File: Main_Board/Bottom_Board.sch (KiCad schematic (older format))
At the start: 18 parts, among them P1 CONN_01X08, P2 CONN_01X08, U2 DYS_mini_ESC, U3 DYS_mini_ESC, U4 DYS_mini_ESC, U5 DYS_mini_ESC, U7 AL8805W5

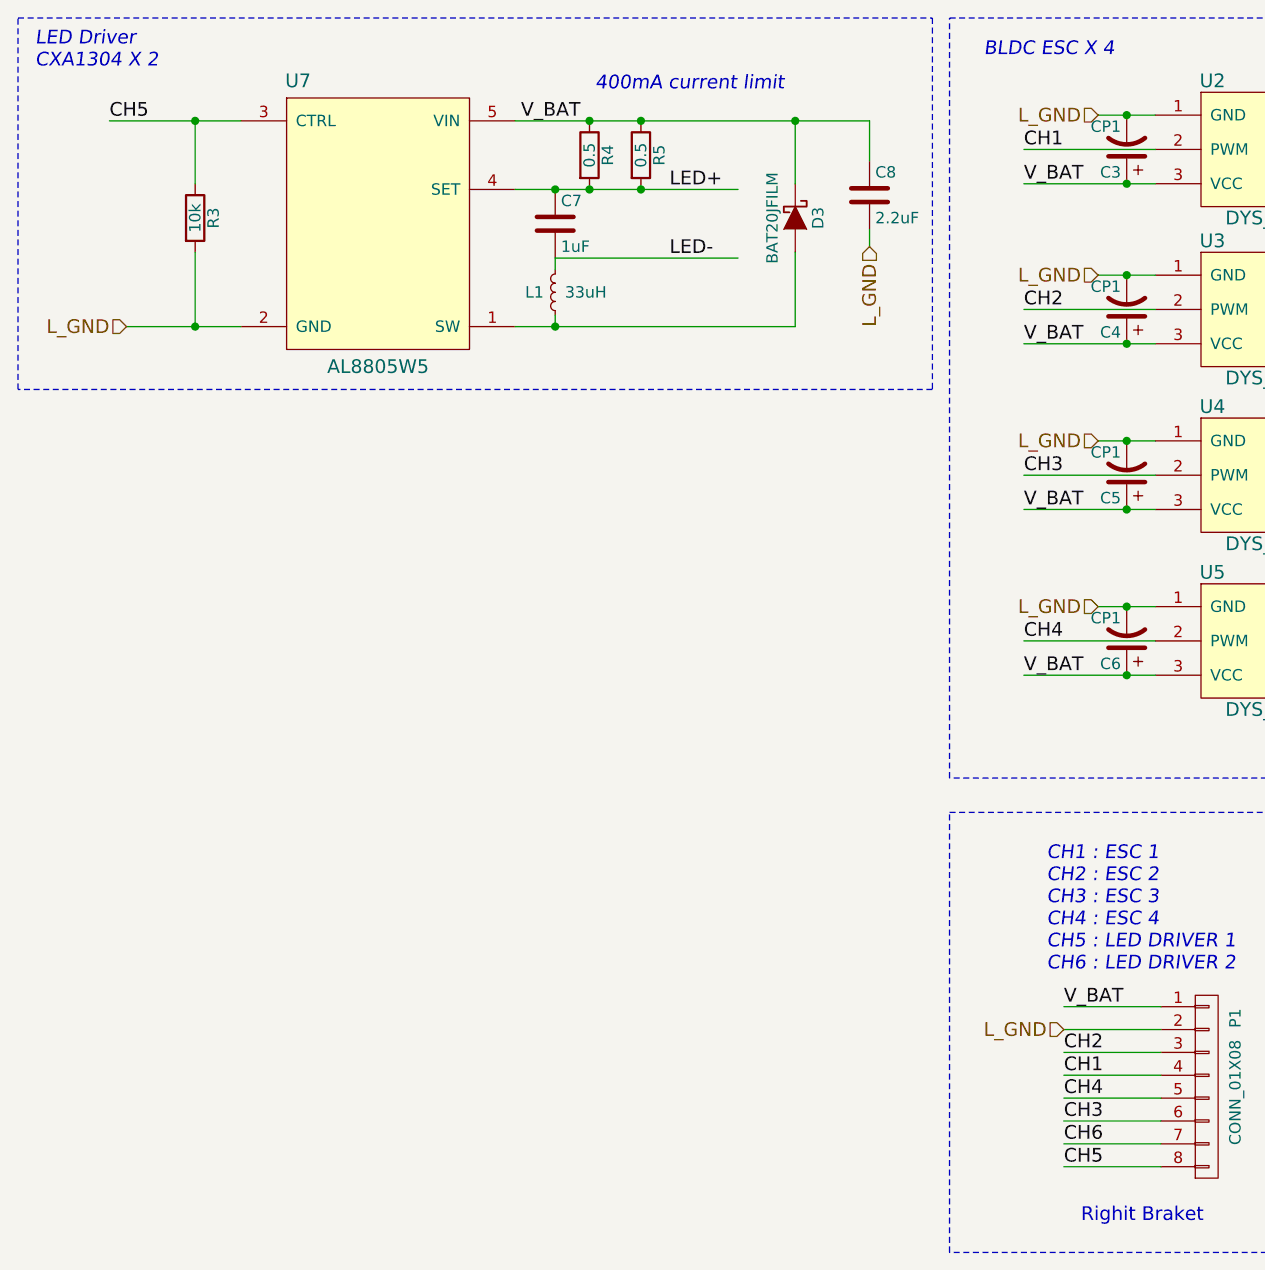
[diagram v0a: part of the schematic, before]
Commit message: Main Board : Recover LED driver USB Dist Board : Delete ADC voltage divider
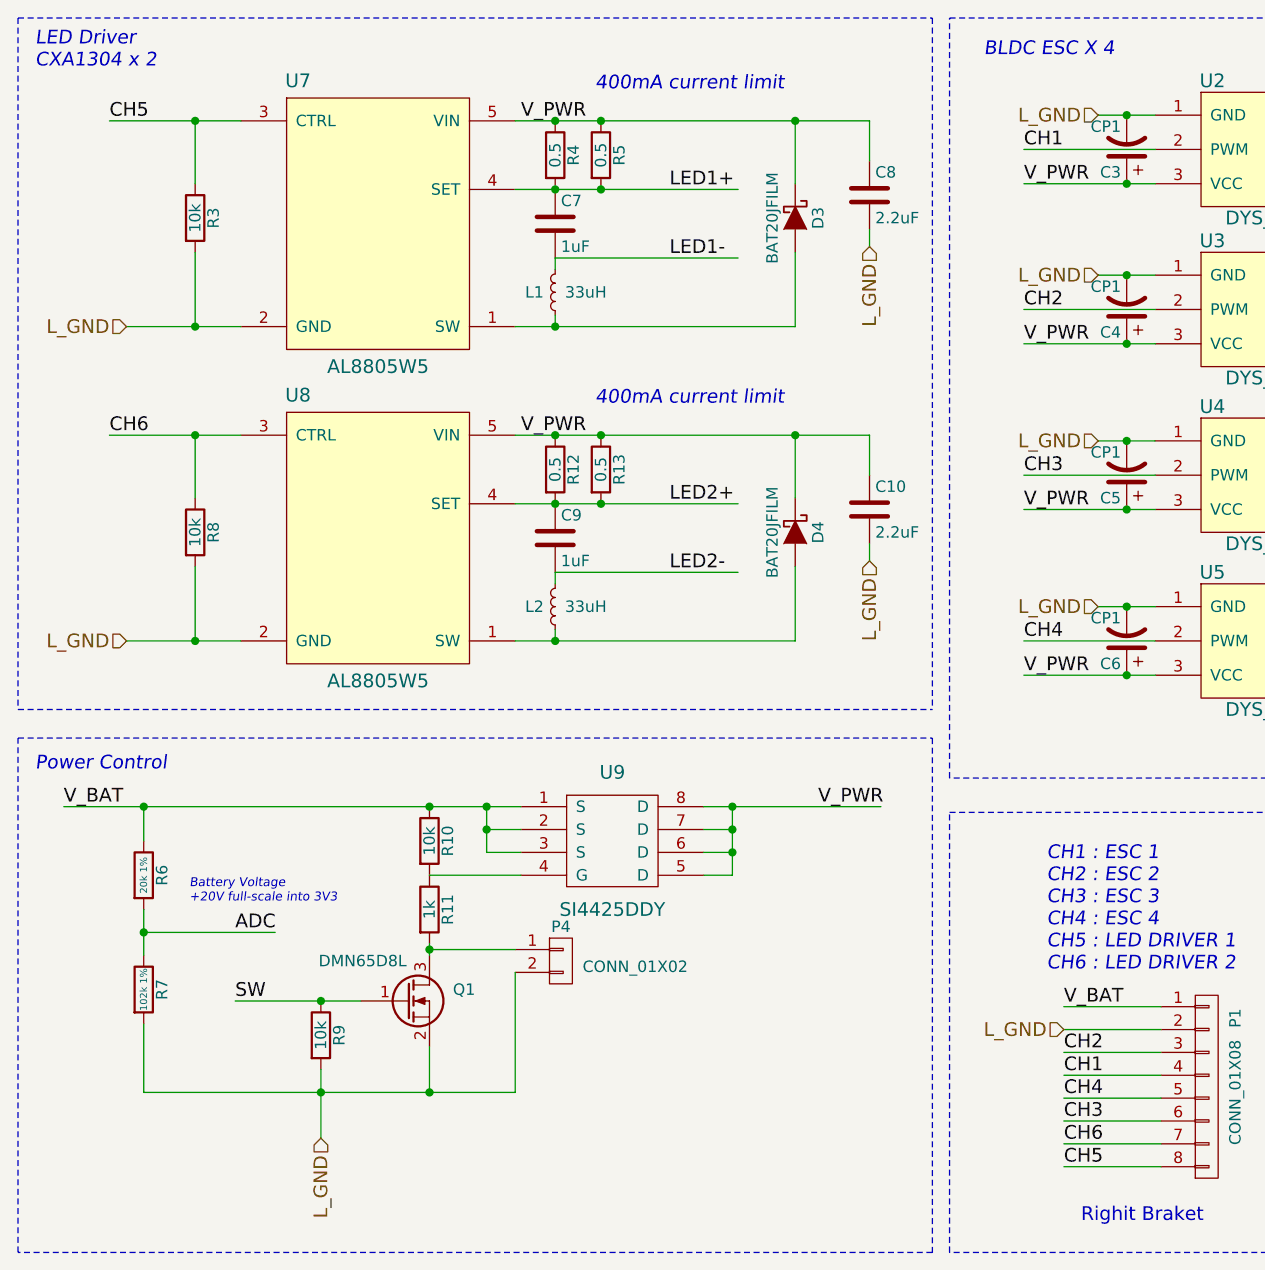
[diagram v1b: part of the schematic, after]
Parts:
- added C10: 2.2uF, Capacitors_SMD:C_0805, symbol C
- added C9: 1uF, Capacitors_SMD:C_0805, symbol C
- added D4: BAT20JFILM, Diodes_SMD:SOD-323_HandSoldering, symbol D_Schottky
- added L2: 33uH, KiCad_Footprint:inductor_33uH, symbol L_Small
- added P4: CONN_01X02, Socket_Strips:Socket_Strip_Straight_1x02, symbol CONN_01X02
- added Q1: DMN65D8L, TO_SOT_Packages_SMD:SOT-23, symbol Q_NMOS_GSD
- added R10, R8, R9: 10k, Capacitors_SMD:C_0603, symbol R
- added R11: 1k, Capacitors_SMD:C_0603, symbol R
- added R12, R13: 0.5, Capacitors_SMD:C_0805, symbol R
- added R6: 20k 1%, Capacitors_SMD:C_0603, symbol R
- added R7: 102k 1%, Capacitors_SMD:C_0603, symbol R
- added U8: AL8805W5, TO_SOT_Packages_SMD:SOT-23-5, symbol AL8805W5
- added U9: SI4425DDY, SMD_Packages:SOIC-8-N, symbol SI4425DDY
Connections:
- net labels added: LED1+, LED1-, LED2+, LED2-, V_PWR
- net labels removed: LED+, LED-
- wire segments 54 -> 89
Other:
- note added: "Battery Voltage\n+20V full-scale into 3V3"
- note added: "LED Driver\nCXA1304 x 2"
- note added: "Power Control"
- note removed: "LED Driver\nCXA1304 X 2"
- moved on the sheet: R4, R5

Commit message: development start
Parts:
- added C11: C, Capacitors_SMD:C_0805, symbol C
- added C12: C, Capacitors_SMD:C_0603, symbol C
- added P5: CONN_01X02, Socket_Strips:Socket_Strip_Straight_1x02, symbol CONN_01X02
- added R14, R15, R16, R17: 10k, Capacitors_SMD:C_0603, symbol R
- added U10: DSN-MINI-360, KiCad_Footprint:DSN-MINI-360, symbol DSN-MINI-360
- added U11: TLV1117LV33, TO_SOT_Packages_SMD:SOT-223, symbol TLV1117LV33
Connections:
- net labels added: 3V3, 5V, GND
- wire segments 89 -> 105
- no-connect marks 0 -> 2
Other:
- note added: "External 5V"
- note added: "Switching Regulator\nMust be replaced.."
- moved on the sheet: C3, C4, C5, C6, U2, U3, U4, U5

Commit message: shit
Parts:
- removed P1, P2: CONN_01X08, Socket_Strips:Socket_Strip_Straight_1x08, symbol CONN_01X08
- added C13, C14: 33uF, Capacitors_SMD:C_0603, symbol C
- added C15, C16, C17, C18: 1uF, Capacitors_SMD:C_0603, symbol C
- added C19, C20: 47pF, Capacitors_SMD:C_0603, symbol C
- added C21: 10uF, Capacitors_SMD:C_0603, symbol C
- added D5: LED, LEDs:LED_0805, symbol LED
- added P1, P2, P7: CONN_01X06, Socket_Strips:Socket_Strip_Straight_1x06, symbol CONN_01X06
- added P10, P11, P12, P9: CONN_01X02, Socket_Strips:Socket_Strip_Straight_1x02, symbol CONN_01X02
- added P13: CONN_02X07, Socket_Strips:Socket_Strip_Straight_2x07, symbol CONN_02X07
- added P14: USB_A, Connect:USB_Mini-B, symbol USB_A
- added P6: BOOT, Socket_Strips:Socket_Strip_Straight_1x02, symbol CONN_01X02
- added P8: CONN_01X04, Socket_Strips:Socket_Strip_Angled_1x04, symbol CONN_01X04
- added Q2: BSS84, TO_SOT_Packages_SMD:SOT-23, symbol Q_PMOS_GSD
- added Q3, Q4: BSS138, TO_SOT_Packages_SMD:SOT-23, symbol BSS138
- added R18: 330, Capacitors_SMD:C_0603, symbol R
- added R19, R20, R21: 10k, Capacitors_SMD:C_0603, symbol R
- added R22: 1.5k, Capacitors_SMD:C_0603, symbol R
- added R23, R24: 22, Capacitors_SMD:C_0603, symbol R
- added RP1, RP2, RP3: 220X4, Resistors_SMD:R_Array_Concave_4x0603, symbol R_PACK4
- added SW1: RESET, KiCad_Footprint:smd_push, symbol SW_PUSH_SMALL_H
- added U12: STM32F103CBT6, Housings_QFP:LQFP-48_7x7mm_Pitch0.5mm, symbol STM32F103CBTx
- added U13: pca9685, Housings_SSOP:TSSOP-28_4.4x9.7mm_Pitch0.65mm, symbol pca9685
- added X1: 8MHz, KiCad_Footprint:crystal_maple, symbol CRYSTAL_SMD
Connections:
- net labels added: BOOT0, D+, D-, D0, D1, D10, D11, D12, D13, D14, D17, D18, D19, D20, D21, D22, D25, D26, D27, D28, D29, D3, D30, D31, D4, D5, D6, D7, D8, D9, DISC, GNDD, GNDPWR, L_C, L_E, L_T+, L_T-, OSC_IN, OSC_OUT, SCL_3V3, SCL_5V, SDA_3V3, SDA_5V, USBDM, USBDP
- net labels removed: 3V3_Front, BOOT, GND, L_GND, SCL, SDA
- wire segments 105 -> 252
- no-connect marks 2 -> 6
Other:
- note added: "16-Channel 12-bit\n5V PWM generator"
- note added: "3.3V to 5V level shifter"
- note added: "Maple Mini Board"
- note added: "Top-Bottom connection"
- note added: "Top-Front connection"
- note removed: "CH1 : ESC 1\nCH2 : ESC 2\nCH3 : ESC 3\nCH4 : ESC 4\nCH5 : LED DRIVER 1\nCH6 : LED DRIVER 2"
- note removed: "Front Board Pin Bridge"
- note removed: "Left Braket"
- note removed: "Righit Braket"
- moved on the sheet: C10, C11, C12, C3, C4, C5, C6, C7, C8, C9, D3, D4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

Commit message: Final Routing
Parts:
- removed C11: C, Capacitors_SMD:C_0805, symbol C
- removed C12: C, Capacitors_SMD:C_0603, symbol C
- removed C13, C14: 33uF, Capacitors_SMD:C_0603, symbol C
- removed C15, C16, C17, C18: 1uF, Capacitors_SMD:C_0603, symbol C
- removed C19, C20: 47pF, Capacitors_SMD:C_0603, symbol C
- removed C21: 10uF, Capacitors_SMD:C_0603, symbol C
- removed D5: LED, LEDs:LED_0805, symbol LED
- removed P1, P2, P7: CONN_01X06, Socket_Strips:Socket_Strip_Straight_1x06, symbol CONN_01X06
- removed P11, P12, P5, P9: CONN_01X02, Socket_Strips:Socket_Strip_Straight_1x02, symbol CONN_01X02
- removed P13: CONN_02X07, Socket_Strips:Socket_Strip_Straight_2x07, symbol CONN_02X07
- removed P14: USB_A, Connect:USB_Mini-B, symbol USB_A
- removed P6: BOOT, Socket_Strips:Socket_Strip_Straight_1x02, symbol CONN_01X02
- removed P8: CONN_01X04, Socket_Strips:Socket_Strip_Angled_1x04, symbol CONN_01X04
- removed Q2: BSS84, TO_SOT_Packages_SMD:SOT-23, symbol Q_PMOS_GSD
- removed Q3, Q4: BSS138, TO_SOT_Packages_SMD:SOT-23, symbol BSS138
- removed R14, R15, R16, R17, R19, R20, R21, R3, R8: 10k, Capacitors_SMD:C_0603, symbol R
- removed R18: 330, Capacitors_SMD:C_0603, symbol R
- removed R22: 1.5k, Capacitors_SMD:C_0603, symbol R
- removed R23, R24: 22, Capacitors_SMD:C_0603, symbol R
- removed R6: 20k 1%, Capacitors_SMD:C_0603, symbol R
- removed R7: 102k 1%, Capacitors_SMD:C_0603, symbol R
- removed RP1, RP2, RP3: 220X4, Resistors_SMD:R_Array_Concave_4x0603, symbol R_PACK4
- removed SW1: RESET, KiCad_Footprint:smd_push, symbol SW_PUSH_SMALL_H
- removed U11: TLV1117LV33, TO_SOT_Packages_SMD:SOT-223, symbol TLV1117LV33
- removed U12: STM32F103CBT6, Housings_QFP:LQFP-48_7x7mm_Pitch0.5mm, symbol STM32F103CBTx
- removed U13: pca9685, Housings_SSOP:TSSOP-28_4.4x9.7mm_Pitch0.65mm, symbol pca9685
- removed X1: 8MHz, KiCad_Footprint:crystal_maple, symbol CRYSTAL_SMD
- added J1: DB25, Connect:DB25FC, symbol DB25
- added P12, P17: CONN_01X03, Socket_Strips:Socket_Strip_Straight_1x03, symbol CONN_01X03
- added P15: CONN_01X07, Socket_Strips:Socket_Strip_Straight_1x07, symbol CONN_01X07
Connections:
- net labels added: PWR_SW, T+, T-
- net labels removed: 3V3, ADC, BOOT0, D+, D-, D0, D1, D10, D11, D12, D13, D14, D17, D18, D19, D20, D21, D22, D25, D26, D27, D28, D29, D3, D30, D31, D4, D5, D6, D7, D8, D9, DISC, GNDD, L_C, L_E, L_T+, L_T-, OSC_IN, OSC_OUT, SCL_3V3, SCL_5V, SDA_3V3, SDA_5V, SW, USBDM, USBDP
- wire segments 252 -> 107
- no-connect marks 6 -> 0
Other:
- note removed: "16-Channel 12-bit\n5V PWM generator"
- note removed: "3.3V to 5V level shifter"
- note removed: "Battery Voltage\n+20V full-scale into 3V3"
- note removed: "External 5V"
- note removed: "Maple Mini Board"
- note removed: "Top-Front connection"

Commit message: Schematic arrangement
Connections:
- no-connect marks 0 -> 5
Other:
- moved on the sheet: J1
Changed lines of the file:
@@
 Text Label 9275 2500 0    60   ~ 0
 CH6
-Text Notes 5775 3025 0    60   Italic 0
+Text Notes 5775 2950 0    60   Italic 0
 Top-Bottom connection
 $Comp
@@
 L DB25 J1
 U 1 1 583A25C9
-P 2925 2325
-F 0 "J1" H 2975 3675 50  0000 C CNN
-F 1 "DB25" H 2875 975 50  0000 C CNN
-F 2 "Connect:DB25FC" H 2925 2325 50  0001 C CNN
-F 3 "" H 2925 2325 50  0000 C CNN
-	1    2925 2325
+P 3675 2975
+F 0 "J1" H 3725 4325 50  0000 C CNN
+F 1 "DB25" H 3625 1625 50  0000 C CNN
+F 2 "Connect:DB25FC" H 3675 2975 50  0001 C CNN
+F 3 "" H 3675 2975 50  0000 C CNN
+	1    3675 2975
 	1    0    0    -1
 $EndComp
-Text Label 1825 1225 0    60   ~ 0
+Text Label 2575 1875 0    60   ~ 0
 MOTOR_1A
-Text Label 1825 1425 0    60   ~ 0
+Text Label 2575 2075 0    60   ~ 0
 MOTOR_1B
-Text Label 1825 1625 0    60   ~ 0
+Text Label 2575 2275 0    60   ~ 0
 MOTOR_1C
-Text Label 1825 1825 0    60   ~ 0
+Text Label 2575 2475 0    60   ~ 0
 MOTOR_2A
-Text Label 1825 2025 0    60   ~ 0
+Text Label 2575 2675 0    60   ~ 0
 MOTOR_2B
-Text Label 1825 2225 0    60   ~ 0
+Text Label 2575 2875 0    60   ~ 0
 MOTOR_2C
 Wire Wire Line
@@
 	7675 1225 8000 1225
 Wire Wire Line
-	2475 1225 1825 1225
-Wire Wire Line
-	2475 1425 1825 1425
-Wire Wire Line
-	2475 1625 1825 1625
-Wire Wire Line
-	2475 1825 1825 1825
-Wire Wire Line
-	2475 2025 1825 2025
-Wire Wire Line
-	2475 2225 1825 2225
-Wire Wire Line
-	2475 1125 1225 1125
-Text Label 1225 1125 0    60   ~ 0
+	3225 1875 2575 1875
+Wire Wire Line
+	3225 2075 2575 2075
+Wire Wire Line
+	3225 2275 2575 2275
+Wire Wire Line
+	3225 2475 2575 2475
+Wire Wire Line
+	3225 2675 2575 2675
+Wire Wire Line
+	3225 2875 2575 2875
+Wire Wire Line
+	3225 1775 1975 1775
+Text Label 1975 1775 0    60   ~ 0
 MOTOR_3A
 Wire Wire Line
-	2475 1325 1225 1325
-Wire Wire Line
-	2475 1525 1225 1525
-Text Label 1225 1325 0    60   ~ 0
+	3225 1975 1975 1975
+Wire Wire Line
+	3225 2175 1975 2175
+Text Label 1975 1975 0    60   ~ 0
 MOTOR_3B
-Text Label 1225 1525 0    60   ~ 0
+Text Label 1975 2175 0    60   ~ 0
 MOTOR_3C
 Wire Wire Line
-	2475 1725 1225 1725
-Wire Wire Line
-	2475 1925 1225 1925
-Wire Wire Line
-	2475 2125 1225 2125
-Text Label 1225 1725 0    60   ~ 0
+	3225 2375 1975 2375
+Wire Wire Line
+	3225 2575 1975 2575
+Wire Wire Line
+	3225 2775 1975 2775
+Text Label 1975 2375 0    60   ~ 0
 MOTOR_4A
-Text Label 1225 1925 0    60   ~ 0
+Text Label 1975 2575 0    60   ~ 0
 MOTOR_4B
-Text Label 1225 2125 0    60   ~ 0
+Text Label 1975 2775 0    60   ~ 0
 MOTOR_4C
 Wire Wire Line
-	2475 2325 1225 2325
-Wire Wire Line
-	2475 2525 1225 2525
-Text Label 1225 2325 0    60   ~ 0
+	3225 2975 1975 2975
+Wire Wire Line
+	3225 3175 1975 3175
+Text Label 1975 2975 0    60   ~ 0
 LED2-
-Text Label 1225 2525 0    60   ~ 0
+Text Label 1975 3175 0    60   ~ 0
 LED2+
 Wire Wire Line
-	2475 2725 1225 2725
-Wire Wire Line
-	2475 2925 1225 2925
-Text Label 1225 2725 0    60   ~ 0
+	3225 3375 1975 3375
+Wire Wire Line
+	3225 3575 1975 3575
+Text Label 1975 3375 0    60   ~ 0
 LED1-
-Text Label 1225 2925 0    60   ~ 0
+Text Label 1975 3575 0    60   ~ 0
 LED1+
 Wire Wire Line
-	2475 3525 1225 3525
-Text Label 1225 3525 0    60   ~ 0
+	3225 4175 1975 4175
+Text Label 1975 4175 0    60   ~ 0
 V_BAT
 Wire Wire Line
-	1300 3325 2475 3325
-$Comp
-L GNDPWR #PWR?
+	2050 3975 3225 3975
+$Comp
+L GNDPWR #PWR015
 U 1 1 583ABF8F
-P 1300 3325
-F 0 "#PWR?" H 1300 3125 50  0001 C CNN
-F 1 "GNDPWR" H 1300 3195 50  0000 C CNN
-F 2 "" H 1300 3275 50  0000 C CNN
-F 3 "" H 1300 3275 50  0000 C CNN
-	1    1300 3325
+P 2050 3975
+F 0 "#PWR015" H 2050 3775 50  0001 C CNN
+F 1 "GNDPWR" H 2050 3845 50  0000 C CNN
+F 2 "" H 2050 3925 50  0000 C CNN
+F 3 "" H 2050 3925 50  0000 C CNN
+	1    2050 3975
 	0    1    1    0
 $EndComp
 Wire Wire Line
-	2475 3225 2200 3225
-Wire Wire Line
-	2200 3225 2200 3325
-Connection ~ 2200 3325
-Wire Wire Line
-	2475 3425 1825 3425
+	3225 3875 2950 3875
+Wire Wire Line
+	2950 3875 2950 3975
+Connection ~ 2950 3975
+Wire Wire Line
+	3225 4075 2575 4075
 Wire Wire Line
 	6350 4300 6625 4300
@@
 	6625 4300 6625 4200
 Connection ~ 6625 4200
-Text Label 1825 3425 0    60   ~ 0
+Text Label 2575 4075 0    60   ~ 0
 T+
+Wire Notes Line
+	5700 2775 8775 2775
+Wire Notes Line
+	8775 2775 8775 5250
+Wire Notes Line
+	8775 5250 5700 5250
+Wire Notes Line
+	5700 5250 5700 2775
+NoConn ~ 3225 3075
+NoConn ~ 3225 3275
+NoConn ~ 3225 3475
+NoConn ~ 3225 3675
+NoConn ~ 3225 3775
 $EndSCHEMATC
